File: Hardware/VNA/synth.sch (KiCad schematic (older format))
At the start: 32 parts, among them U1 MAX2871, X1 ASTXR-12-19.200MHz

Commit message: added footprints and 3d models
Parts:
- U1: footprint (none) -> VNA_Footprints:QFN-32-1EP_5x5mm_Pitch0.5mm_Thermal_Vias
- X1: footprint (none) -> VNA_Footprints:ASTXR-12
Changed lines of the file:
@@
 F 0 "X1" H 1600 3425 50  0000 C CNN
 F 1 "ASTXR-12-19.200MHz" H 1600 3334 50  0000 C CNN
-F 2 "" H 1400 3300 50  0001 C CNN
+F 2 "VNA_Footprints:ASTXR-12" H 1400 3300 50  0001 C CNN
 F 3 "" H 1400 3300 50  0001 C CNN
 	1    1500 3150
@@
 F 0 "U1" H 3650 5650 50  0000 C CNN
 F 1 "MAX2871" H 3750 5550 50  0000 C CNN
-F 2 "" H 5600 5800 50  0001 L CNN
+F 2 "VNA_Footprints:QFN-32-1EP_5x5mm_Pitch0.5mm_Thermal_Vias" H 5600 5800 50  0001 L CNN
 F 3 "https://componentsearchengine.com/Datasheets/1/MAX2871ETJ+.pdf" H 4850 5550 50  0001 L CNN
 	1    4400 4650

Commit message: prelim schematic capture complete
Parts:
- removed FB1, FB2: BLM18PG181SN1D, VNA_Footprints:BEADC1608X95N, symbol Device:Ferrite_Bead
- added FB2, FB3: Bead, symbol VNA_Symbols:Ferrite_Bead_PWR
- renumbered C8 to C10, C9 to C11, C10 to C12, C11 to C13, C12 to C14, C13 to C15, C14 to C16, C15 to C17, C16 to C18, C17 to C19, C18 to C20, C19 to C21, C20 to C22, C21 to C23, C22 to C24, C23 to C25, C24 to C26, C25 to C27, C5 to C7, C6 to C8, C7 to C9, R9 to R10, R10 to R11, R11 to R12, R5 to R6, R6 to R7, R7 to R8, R8 to R9, U1 to U3
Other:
- note added: "MAX2871: 23.5 - 6000 MHz PLL\n"
- note removed: "MAX2871 23.5 - 6000 MHz PLL\n"

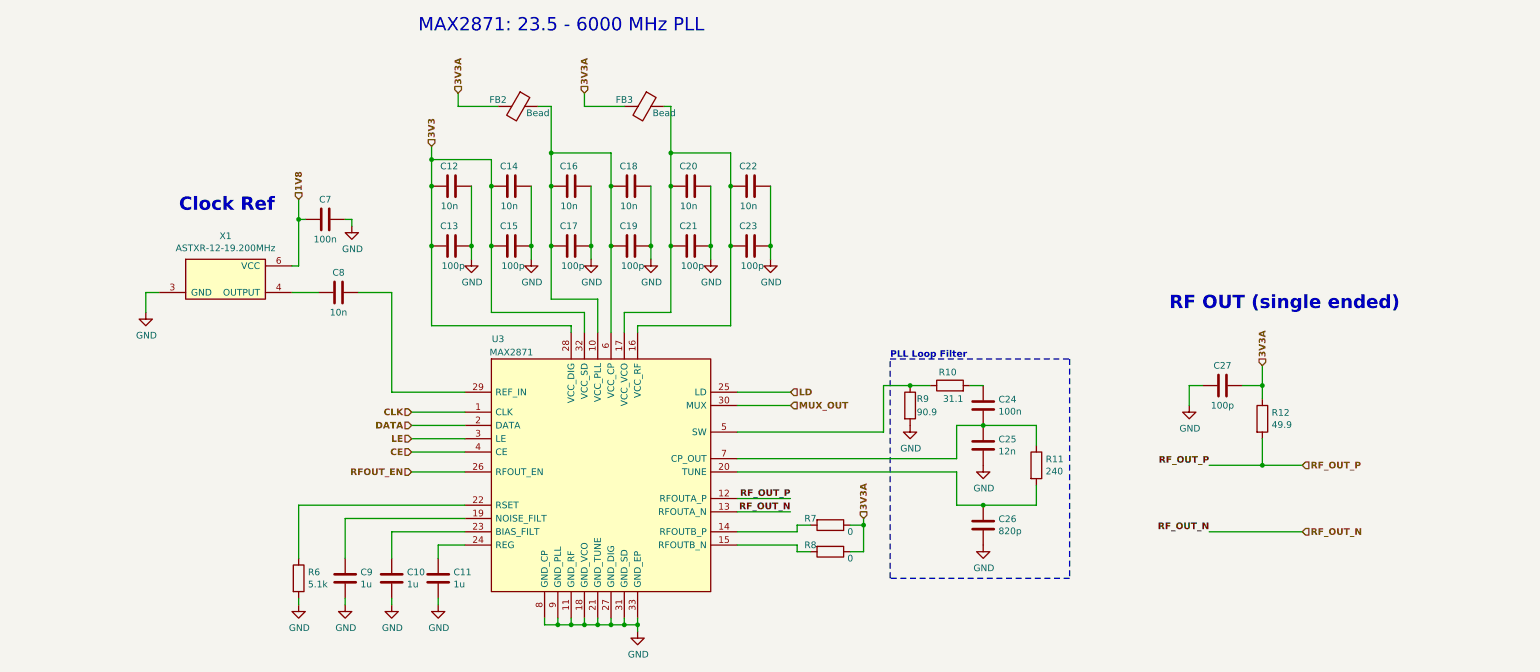
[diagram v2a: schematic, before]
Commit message: all 3d models created, prelim bom generated
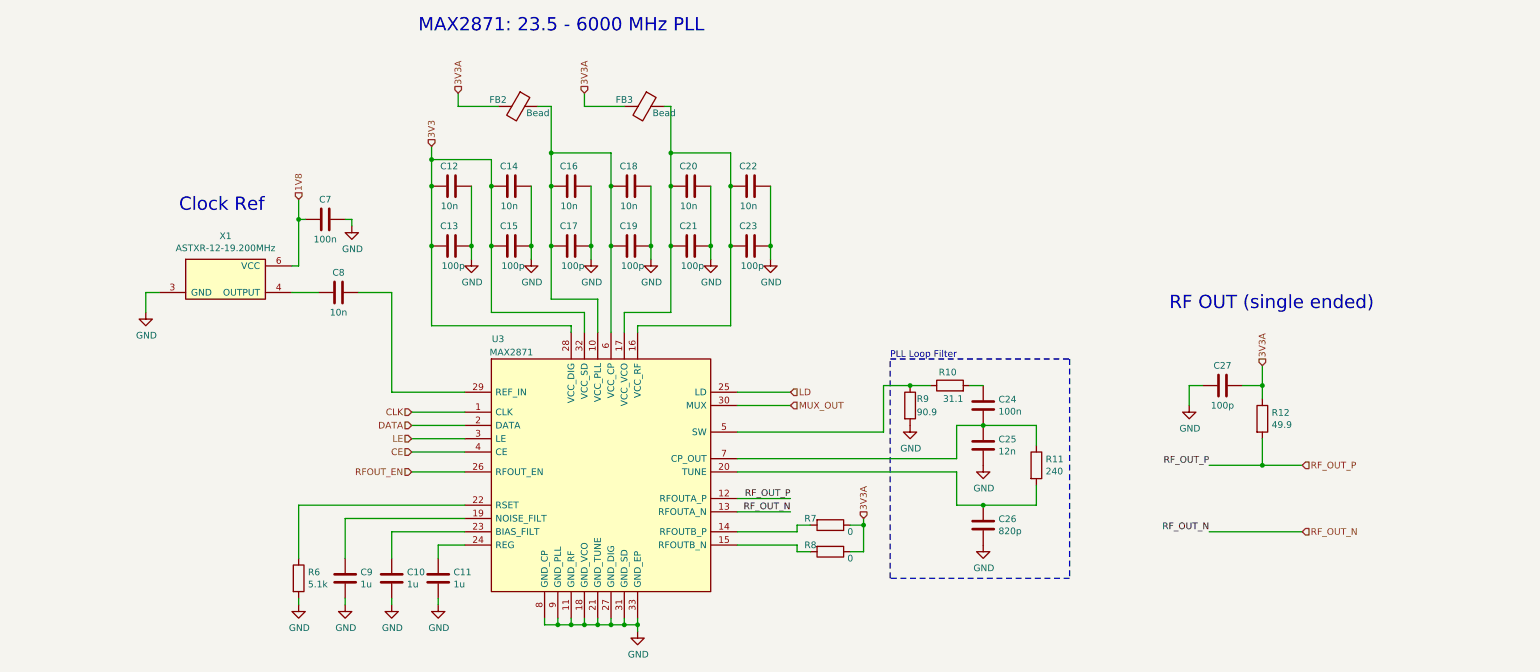
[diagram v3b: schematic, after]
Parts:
- FB2, FB3: footprint (none) -> VNA_Footprints:BEADC1608X95N
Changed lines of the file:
@@
 Wire Notes Line
 	6600 5450 6600 3800
-Text Notes 6600 3800 0    50   ~ 6
+Text Notes 6600 3800 0    50   ~ 0
 PLL Loop Filter\n
 Wire Wire Line
@@
 Wire Wire Line
 	5450 4950 5850 4950
-Text Label 5850 4950 2    50   ~ 6
+Text Label 5850 4950 2    50   ~ 0
 RF_OUT_N
-Text Label 5850 4850 2    50   ~ 6
+Text Label 5850 4850 2    50   ~ 0
 RF_OUT_P
 Wire Wire Line
@@
 	4950 1900 4950 2250
 Connection ~ 4950 2250
-Text Label 9000 5100 2    50   ~ 6
+Text Label 9000 5100 2    50   ~ 0
 RF_OUT_N
-Text Label 9000 4600 2    50   ~ 6
+Text Label 9000 4600 2    50   ~ 0
 RF_OUT_P
 Wire Wire Line
@@
 Wire Wire Line
 	5450 5100 5900 5100
-Text Notes 8700 3600 0    100  ~ 6
+Text Notes 8700 3600 0    100  ~ 0
 RF OUT (single ended)\n\n
 Wire Wire Line
@@
 	1    0    0    -1
 $EndComp
-Text Notes 1250 2700 0    100  ~ 6
+Text Notes 1250 2700 0    100  ~ 0
 Clock Ref\n
 Wire Wire Line
@@
 Wire Wire Line
 	3150 2300 3150 2500
-Text HLabel 9700 4600 2    50   Input ~ 6
+Text HLabel 9700 4600 2    50   Input ~ 0
 RF_OUT_P
-Text HLabel 9700 5100 2    50   Input ~ 6
+Text HLabel 9700 5100 2    50   Input ~ 0
 RF_OUT_N
-Text HLabel 5850 4050 2    50   Input ~ 6
+Text HLabel 5850 4050 2    50   Input ~ 0
 LD
-Text HLabel 5850 4150 2    50   Input ~ 6
+Text HLabel 5850 4150 2    50   Input ~ 0
 MUX_OUT
-Text HLabel 3000 4200 0    50   Input ~ 6
+Text HLabel 3000 4200 0    50   Input ~ 0
 CLK
-Text HLabel 3000 4300 0    50   Input ~ 6
+Text HLabel 3000 4300 0    50   Input ~ 0
 DATA
-Text HLabel 3000 4400 0    50   Input ~ 6
+Text HLabel 3000 4400 0    50   Input ~ 0
 LE
-Text HLabel 3000 4500 0    50   Input ~ 6
+Text HLabel 3000 4500 0    50   Input ~ 0
 CE
-Text HLabel 3000 4650 0    50   Input ~ 6
+Text HLabel 3000 4650 0    50   Input ~ 0
 RFOUT_EN
 Connection ~ 3150 2500
@@
 Text Notes 3050 1350 0    100  ~ 0
 MAX2871: 23.5 - 6000 MHz PLL\n
-Text HLabel 9400 3850 1    50   Input ~ 6
+Text HLabel 9400 3850 1    50   Input ~ 0
 3V3A
-Text HLabel 2150 2600 1    50   Input ~ 6
+Text HLabel 2150 2600 1    50   Input ~ 0
 1V8
-Text HLabel 3350 1800 1    50   Input ~ 6
+Text HLabel 3350 1800 1    50   Input ~ 0
 3V3A
-Text HLabel 4300 1800 1    50   Input ~ 6
+Text HLabel 4300 1800 1    50   Input ~ 0
 3V3A
-Text HLabel 6400 5000 1    50   Input ~ 6
+Text HLabel 6400 5000 1    50   Input ~ 0
 3V3A
-Text HLabel 3150 2200 1    50   Input ~ 6
+Text HLabel 3150 2200 1    50   Input ~ 0
 3V3
 $Comp
@@
 F 0 "FB2" V 3750 1750 50  0000 C CNN
 F 1 "Bead" V 3850 2050 50  0000 C CNN
-F 2 "" V 3730 1900 50  0001 C CNN
+F 2 "VNA_Footprints:BEADC1608X95N" V 3730 1900 50  0001 C CNN
 F 3 "~" H 3800 1900 50  0001 C CNN
 	1    3800 1900
@@
 F 0 "FB3" V 4700 1750 50  0000 C CNN
 F 1 "Bead" V 4800 2050 50  0000 C CNN
-F 2 "" V 4680 1900 50  0001 C CNN
+F 2 "VNA_Footprints:BEADC1608X95N" V 4680 1900 50  0001 C CNN
 F 3 "~" H 4750 1900 50  0001 C CNN
 	1    4750 1900

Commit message: More schematic changes + updated functionals
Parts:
- added C?: DNP, symbol Device:C
- added R?: DNP, symbol Device:R
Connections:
- net GND: now also R?.2
- net at C26.1, U3.20 (TUNE): now also R11.1; no longer R11.2
- net at C24.2, C25.1, U3.7 (CP_OUT): now also R11.2, C?.1; no longer R11.1
- new net: C?.2, R?.1
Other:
- note added: "DNP allow for ADF4351\nto replace MAX2871"
- moved on the sheet: C26, C27, R11, R12
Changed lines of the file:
@@
 L Device:C C26
 U 1 1 5C44DD06
-P 7300 5050
-F 0 "C26" H 7415 5096 50  0000 L CNN
-F 1 "820p" H 7415 5005 50  0000 L CNN
-F 2 "Capacitor_SMD:C_0402_1005Metric" H 7338 4900 50  0001 C CNN
-F 3 "~" H 7300 5050 50  0001 C CNN
-	1    7300 5050
+P 8550 4500
+F 0 "C26" H 8665 4546 50  0000 L CNN
+F 1 "820p" H 8665 4455 50  0000 L CNN
+F 2 "Capacitor_SMD:C_0402_1005Metric" H 8588 4350 50  0001 C CNN
+F 3 "~" H 8550 4500 50  0001 C CNN
+	1    8550 4500
 	1    0    0    -1
 $EndComp
@@
 L power:GND #PWR027
 U 1 1 5C44DD0E
-P 7300 5200
-F 0 "#PWR027" H 7300 4950 50  0001 C CNN
-F 1 "GND" H 7305 5027 50  0000 C CNN
-F 2 "" H 7300 5200 50  0001 C CNN
-F 3 "" H 7300 5200 50  0001 C CNN
-	1    7300 5200
+P 8550 4650
+F 0 "#PWR027" H 8550 4400 50  0001 C CNN
+F 1 "GND" H 8555 4477 50  0000 C CNN
+F 2 "" H 8550 4650 50  0001 C CNN
+F 3 "" H 8550 4650 50  0001 C CNN
+	1    8550 4650
 	1    0    0    -1
 $EndComp
@@
 L Device:R R11
 U 1 1 5C45B711
-P 7700 4600
-F 0 "R11" H 7770 4646 50  0000 L CNN
-F 1 "240" H 7770 4555 50  0000 L CNN
-F 2 "Resistor_SMD:R_0402_1005Metric" V 7630 4600 50  0001 C CNN
-F 3 "~" H 7700 4600 50  0001 C CNN
-	1    7700 4600
-	1    0    0    -1
-$EndComp
-Wire Wire Line
-	7700 4300 7700 4450
+P 8200 4300
+F 0 "R11" V 8100 4200 50  0000 L CNN
+F 1 "240" V 8300 4200 50  0000 L CNN
+F 2 "Resistor_SMD:R_0402_1005Metric" V 8130 4300 50  0001 C CNN
+F 3 "~" H 8200 4300 50  0001 C CNN
+	1    8200 4300
+	0    1    1    0
+$EndComp
 Wire Wire Line
 	7100 4550 7100 4300
-Wire Wire Line
-	7100 4900 7100 4650
-Wire Wire Line
-	7700 4900 7700 4750
 Wire Wire Line
 	6550 4000 6550 4350
 Wire Notes Line
-	6600 3800 7950 3800
-Wire Notes Line
-	7950 3800 7950 5450
-Wire Notes Line
-	7950 5450 6600 5450
-Wire Notes Line
-	6600 5450 6600 3800
-Text Notes 6600 3800 0    50   ~ 0
+	6600 5400 6600 3800
+Text Notes 6600 3800 0    50   ~ 6
 PLL Loop Filter\n
 Wire Wire Line
@@
 Wire Wire Line
 	5450 4950 5850 4950
-Text Label 5850 4950 2    50   ~ 0
+Text Label 5850 4950 2    50   ~ 6
 RF_OUT_N
-Text Label 5850 4850 2    50   ~ 0
+Text Label 5850 4850 2    50   ~ 6
 RF_OUT_P
 Wire Wire Line
@@
 	4950 1900 4950 2250
 Connection ~ 4950 2250
-Text Label 9000 5100 2    50   ~ 0
+Text Label 9600 5100 2    50   ~ 6
 RF_OUT_N
-Text Label 9000 4600 2    50   ~ 0
+Text Label 9600 4600 2    50   ~ 6
 RF_OUT_P
 Wire Wire Line
@@
 L Device:R R12
 U 1 1 5C664064
-P 9400 4250
-F 0 "R12" H 9470 4296 50  0000 L CNN
-F 1 "49.9" H 9470 4205 50  0000 L CNN
-F 2 "Resistor_SMD:R_0402_1005Metric" V 9330 4250 50  0001 C CNN
-F 3 "~" H 9400 4250 50  0001 C CNN
-	1    9400 4250
+P 10000 4250
+F 0 "R12" H 10070 4296 50  0000 L CNN
+F 1 "49.9" H 10070 4205 50  0000 L CNN
+F 2 "Resistor_SMD:R_0402_1005Metric" V 9930 4250 50  0001 C CNN
+F 3 "~" H 10000 4250 50  0001 C CNN
+	1    10000 4250
 	1    0    0    -1
 $EndComp
@@
 L Device:C C27
 U 1 1 5C674D87
-P 9100 4000
-F 0 "C27" V 8950 4000 50  0000 C CNN
-F 1 "100p" V 9250 4000 50  0000 C CNN
-F 2 "Capacitor_SMD:C_0402_1005Metric" H 9138 3850 50  0001 C CNN
-F 3 "~" H 9100 4000 50  0001 C CNN
-	1    9100 4000
-	0    1    1    0
-$EndComp
-Wire Wire Line
-	9250 4000 9400 4000
-Wire Wire Line
-	8950 4000 8850 4000
-Wire Wire Line
-	8850 4000 8850 4150
+P 9700 4000
+F 0 "C27" V 9550 4000 50  0000 C CNN
+F 1 "100p" V 9850 4000 50  0000 C CNN
+F 2 "Capacitor_SMD:C_0402_1005Metric" H 9738 3850 50  0001 C CNN
+F 3 "~" H 9700 4000 50  0001 C CNN
+	1    9700 4000
+	0    1    1    0
+$EndComp
+Wire Wire Line
+	9850 4000 10000 4000
+Wire Wire Line
+	9550 4000 9450 4000
+Wire Wire Line
+	9450 4000 9450 4150
 $Comp
 L power:GND #PWR028
 U 1 1 5C6A88A2
-P 8850 4150
-F 0 "#PWR028" H 8850 3900 50  0001 C CNN
-F 1 "GND" H 8855 3977 50  0000 C CNN
-F 2 "" H 8850 4150 50  0001 C CNN
-F 3 "" H 8850 4150 50  0001 C CNN
-	1    8850 4150
-	1    0    0    -1
-$EndComp
-Connection ~ 9400 4000
-Wire Wire Line
-	9400 4000 9400 4100
-Wire Wire Line
-	9400 3850 9400 4000
+P 9450 4150
+F 0 "#PWR028" H 9450 3900 50  0001 C CNN
+F 1 "GND" H 9455 3977 50  0000 C CNN
+F 2 "" H 9450 4150 50  0001 C CNN
+F 3 "" H 9450 4150 50  0001 C CNN
+	1    9450 4150
+	1    0    0    -1
+$EndComp
+Connection ~ 10000 4000
+Wire Wire Line
+	10000 4000 10000 4100
+Wire Wire Line
+	10000 3850 10000 4000
 Wire Wire Line
 	3350 1900 3350 1800
@@
 Wire Wire Line
 	5450 5100 5900 5100
-Text Notes 8700 3600 0    100  ~ 0
+Text Notes 9300 3600 0    100  ~ 6
 RF OUT (single ended)\n\n
 Wire Wire Line
@@
 	1    0    0    -1
 $EndComp
-Text Notes 1250 2700 0    100  ~ 0
+Text Notes 1250 2700 0    100  ~ 6
 Clock Ref\n
 Wire Wire Line
@@
 $EndComp
 Wire Wire Line
-	9000 4600 9400 4600
+	9600 4600 10000 4600
 $Comp
 L VNA_Symbols:ASTXR-12-19.200MHz X1
@@
 $EndComp
 Wire Wire Line
-	9000 5100 9700 5100
-Wire Wire Line
-	9400 4400 9400 4600
-Connection ~ 9400 4600
-Wire Wire Line
-	9400 4600 9700 4600
+	9600 5100 10300 5100
+Wire Wire Line
+	10000 4400 10000 4600
+Connection ~ 10000 4600
+Wire Wire Line
+	10000 4600 10300 4600
 Wire Wire Line
 	3900 2500 3900 2950
@@
 	7100 4300 7300 4300
 Wire Wire Line
-	7100 4900 7300 4900
-Wire Wire Line
 	6550 4000 6750 4000
 Wire Wire Line
@@
 Wire Wire Line
 	3150 2300 3150 2500
-Text HLabel 9700 4600 2    50   Input ~ 0
+Text HLabel 10300 4600 2    50   Input ~ 6
 RF_OUT_P
-Text HLabel 9700 5100 2    50   Input ~ 0
+Text HLabel 10300 5100 2    50   Input ~ 6
 RF_OUT_N
-Text HLabel 5850 4050 2    50   Input ~ 0
+Text HLabel 5850 4050 2    50   Input ~ 6
 LD
-Text HLabel 5850 4150 2    50   Input ~ 0
+Text HLabel 5850 4150 2    50   Input ~ 6
 MUX_OUT
-Text HLabel 3000 4200 0    50   Input ~ 0
+Text HLabel 3000 4200 0    50   Input ~ 6
 CLK
-Text HLabel 3000 4300 0    50   Input ~ 0
+Text HLabel 3000 4300 0    50   Input ~ 6
 DATA
-Text HLabel 3000 4400 0    50   Input ~ 0
+Text HLabel 3000 4400 0    50   Input ~ 6
 LE
-Text HLabel 3000 4500 0    50   Input ~ 0
+Text HLabel 3000 4500 0    50   Input ~ 6
 CE
-Text HLabel 3000 4650 0    50   Input ~ 0
+Text HLabel 3000 4650 0    50   Input ~ 6
 RFOUT_EN
 Connection ~ 3150 2500
@@
 	6750 4000 6900 4000
 Connection ~ 7300 4300
-Wire Wire Line
-	7300 4300 7700 4300
-Connection ~ 7300 4900
-Wire Wire Line
-	7300 4900 7700 4900
-Text Notes 3050 1350 0    100  ~ 0
+Text Notes 3050 1350 0    100  ~ 6
 MAX2871: 23.5 - 6000 MHz PLL\n
-Text HLabel 9400 3850 1    50   Input ~ 0
+Text HLabel 10000 3850 1    50   Input ~ 6
 3V3A
-Text HLabel 2150 2600 1    50   Input ~ 0
+Text HLabel 2150 2600 1    50   Input ~ 6
 1V8
-Text HLabel 3350 1800 1    50   Input ~ 0
+Text HLabel 3350 1800 1    50   Input ~ 6
 3V3A
-Text HLabel 4300 1800 1    50   Input ~ 0
+Text HLabel 4300 1800 1    50   Input ~ 6
 3V3A
-Text HLabel 6400 5000 1    50   Input ~ 0
+Text HLabel 6400 5000 1    50   Input ~ 6
 3V3A
-Text HLabel 3150 2200 1    50   Input ~ 0
+Text HLabel 3150 2200 1    50   Input ~ 6
 3V3
 $Comp
@@
 	0    1    1    0
 $EndComp
+Wire Wire Line
+	7300 4300 7850 4300
+$Comp
+L Device:C C?
+U 1 1 5CB618D9
+P 7850 4500
+F 0 "C?" H 7965 4546 50  0000 L CNN
+F 1 "DNP" H 7965 4455 50  0000 L CNN
+F 2 "" H 7888 4350 50  0001 C CNN
+F 3 "~" H 7850 4500 50  0001 C CNN
+	1    7850 4500
+	1    0    0    -1
+$EndComp
+$Comp
+L Device:R R?
+U 1 1 5CB620B8
+P 7850 4850
+F 0 "R?" H 7920 4896 50  0000 L CNN
+F 1 "DNP" H 7920 4805 50  0000 L CNN
+F 2 "" V 7780 4850 50  0001 C CNN
+F 3 "~" H 7850 4850 50  0001 C CNN
+	1    7850 4850
+	1    0    0    -1
+$EndComp
+Wire Wire Line
+	8550 4300 8550 4350
+Connection ~ 8550 4300
+Wire Wire Line
+	8550 4300 8350 4300
+Wire Wire Line
+	7850 4300 7850 4350
+Connection ~ 7850 4300
+Wire Wire Line
+	7850 4300 8050 4300
+Wire Wire Line
+	7850 4650 7850 4700
+Wire Wire Line
+	7850 5000 7850 5050
+Wire Wire Line
+	9000 4300 9000 5250
+Wire Wire Line
+	9000 5250 7100 5250
+Wire Wire Line
+	7100 4650 7100 5250
+Wire Wire Line
+	8550 4300 9000 4300
+$Comp
+L power:GND #PWR?
+U 1 1 5CB860A2
+P 7850 5050
+F 0 "#PWR?" H 7850 4800 50  0001 C CNN
+F 1 "GND" H 7850 4900 50  0000 C CNN
+F 2 "" H 7850 5050 50  0001 C CNN
+F 3 "" H 7850 5050 50  0001 C CNN
+	1    7850 5050
+	1    0    0    -1
+$EndComp
+Wire Notes Line
+	6600 3800 9100 3800
+Wire Notes Line
+	9100 3800 9100 5400
+Wire Notes Line
+	9100 5400 6600 5400
+Text Notes 8000 5150 0    50   ~ 6
+DNP allow for ADF4351\nto replace MAX2871
 $EndSCHEMATC

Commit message: first day of layout / routing done
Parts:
- C74: renamed from C?; footprint (none) -> Capacitor_SMD:C_0402_1005Metric
- R62: renamed from R?; footprint (none) -> Resistor_SMD:R_0402_1005Metric
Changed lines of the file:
@@
 Wire Notes Line
 	6600 5400 6600 3800
-Text Notes 6600 3800 0    50   ~ 6
+Text Notes 6600 3800 0    50   ~ 10
 PLL Loop Filter\n
 Wire Wire Line
@@
 Wire Wire Line
 	5450 4950 5850 4950
-Text Label 5850 4950 2    50   ~ 6
+Text Label 5850 4950 2    50   ~ 10
 RF_OUT_N
-Text Label 5850 4850 2    50   ~ 6
+Text Label 5850 4850 2    50   ~ 10
 RF_OUT_P
 Wire Wire Line
@@
 	4950 1900 4950 2250
 Connection ~ 4950 2250
-Text Label 9600 5100 2    50   ~ 6
+Text Label 9600 5100 2    50   ~ 10
 RF_OUT_N
-Text Label 9600 4600 2    50   ~ 6
+Text Label 9600 4600 2    50   ~ 10
 RF_OUT_P
 Wire Wire Line
@@
 Wire Wire Line
 	5450 5100 5900 5100
-Text Notes 9300 3600 0    100  ~ 6
+Text Notes 9300 3600 0    100  ~ 20
 RF OUT (single ended)\n\n
 Wire Wire Line
@@
 	1    0    0    -1
 $EndComp
-Text Notes 1250 2700 0    100  ~ 6
+Text Notes 1250 2700 0    100  ~ 20
 Clock Ref\n
 Wire Wire Line
@@
 Wire Wire Line
 	3150 2300 3150 2500
-Text HLabel 10300 4600 2    50   Input ~ 6
+Text HLabel 10300 4600 2    50   Input ~ 10
 RF_OUT_P
-Text HLabel 10300 5100 2    50   Input ~ 6
+Text HLabel 10300 5100 2    50   Input ~ 10
 RF_OUT_N
-Text HLabel 5850 4050 2    50   Input ~ 6
+Text HLabel 5850 4050 2    50   Input ~ 10
 LD
-Text HLabel 5850 4150 2    50   Input ~ 6
+Text HLabel 5850 4150 2    50   Input ~ 10
 MUX_OUT
-Text HLabel 3000 4200 0    50   Input ~ 6
+Text HLabel 3000 4200 0    50   Input ~ 10
 CLK
-Text HLabel 3000 4300 0    50   Input ~ 6
+Text HLabel 3000 4300 0    50   Input ~ 10
 DATA
-Text HLabel 3000 4400 0    50   Input ~ 6
+Text HLabel 3000 4400 0    50   Input ~ 10
 LE
-Text HLabel 3000 4500 0    50   Input ~ 6
+Text HLabel 3000 4500 0    50   Input ~ 10
 CE
-Text HLabel 3000 4650 0    50   Input ~ 6
+Text HLabel 3000 4650 0    50   Input ~ 10
 RFOUT_EN
 Connection ~ 3150 2500
@@
 	6750 4000 6900 4000
 Connection ~ 7300 4300
-Text Notes 3050 1350 0    100  ~ 6
+Text Notes 3050 1350 0    100  ~ 20
 MAX2871: 23.5 - 6000 MHz PLL\n
-Text HLabel 10000 3850 1    50   Input ~ 6
+Text HLabel 10000 3850 1    50   Input ~ 10
 3V3A
-Text HLabel 2150 2600 1    50   Input ~ 6
+Text HLabel 2150 2600 1    50   Input ~ 10
 1V8
-Text HLabel 3350 1800 1    50   Input ~ 6
+Text HLabel 3350 1800 1    50   Input ~ 10
 3V3A
-Text HLabel 4300 1800 1    50   Input ~ 6
+Text HLabel 4300 1800 1    50   Input ~ 10
 3V3A
-Text HLabel 6400 5000 1    50   Input ~ 6
+Text HLabel 6400 5000 1    50   Input ~ 10
 3V3A
-Text HLabel 3150 2200 1    50   Input ~ 6
+Text HLabel 3150 2200 1    50   Input ~ 10
 3V3
 $Comp
@@
 	7300 4300 7850 4300
 $Comp
-L Device:C C?
+L Device:C C74
 U 1 1 5CB618D9
 P 7850 4500
-F 0 "C?" H 7965 4546 50  0000 L CNN
+F 0 "C74" H 7965 4546 50  0000 L CNN
 F 1 "DNP" H 7965 4455 50  0000 L CNN
-F 2 "" H 7888 4350 50  0001 C CNN
+F 2 "Capacitor_SMD:C_0402_1005Metric" H 7888 4350 50  0001 C CNN
 F 3 "~" H 7850 4500 50  0001 C CNN
 	1    7850 4500
@@
 $EndComp
 $Comp
-L Device:R R?
+L Device:R R62
 U 1 1 5CB620B8
 P 7850 4850
-F 0 "R?" H 7920 4896 50  0000 L CNN
+F 0 "R62" H 7920 4896 50  0000 L CNN
 F 1 "DNP" H 7920 4805 50  0000 L CNN
-F 2 "" V 7780 4850 50  0001 C CNN
+F 2 "Resistor_SMD:R_0402_1005Metric" V 7780 4850 50  0001 C CNN
 F 3 "~" H 7850 4850 50  0001 C CNN
 	1    7850 4850
@@
 	8550 4300 9000 4300
 $Comp
-L power:GND #PWR?
+L power:GND #PWR0124
 U 1 1 5CB860A2
 P 7850 5050
-F 0 "#PWR?" H 7850 4800 50  0001 C CNN
+F 0 "#PWR0124" H 7850 4800 50  0001 C CNN
 F 1 "GND" H 7850 4900 50  0000 C CNN
 F 2 "" H 7850 5050 50  0001 C CNN
@@
 Wire Notes Line
 	9100 5400 6600 5400
-Text Notes 8000 5150 0    50   ~ 6
+Text Notes 8000 5150 0    50   ~ 10
 DNP allow for ADF4351\nto replace MAX2871
 $EndSCHEMATC
